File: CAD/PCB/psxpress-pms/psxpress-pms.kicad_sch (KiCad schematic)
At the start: 41 parts, among them IC1 BQ25606RGER, IC2 MAX16054AZT+T, IC3 TPS61023DRLT, IC4 TPS564255DRLR, Q1 AONR21117, SW1 SW_SPST

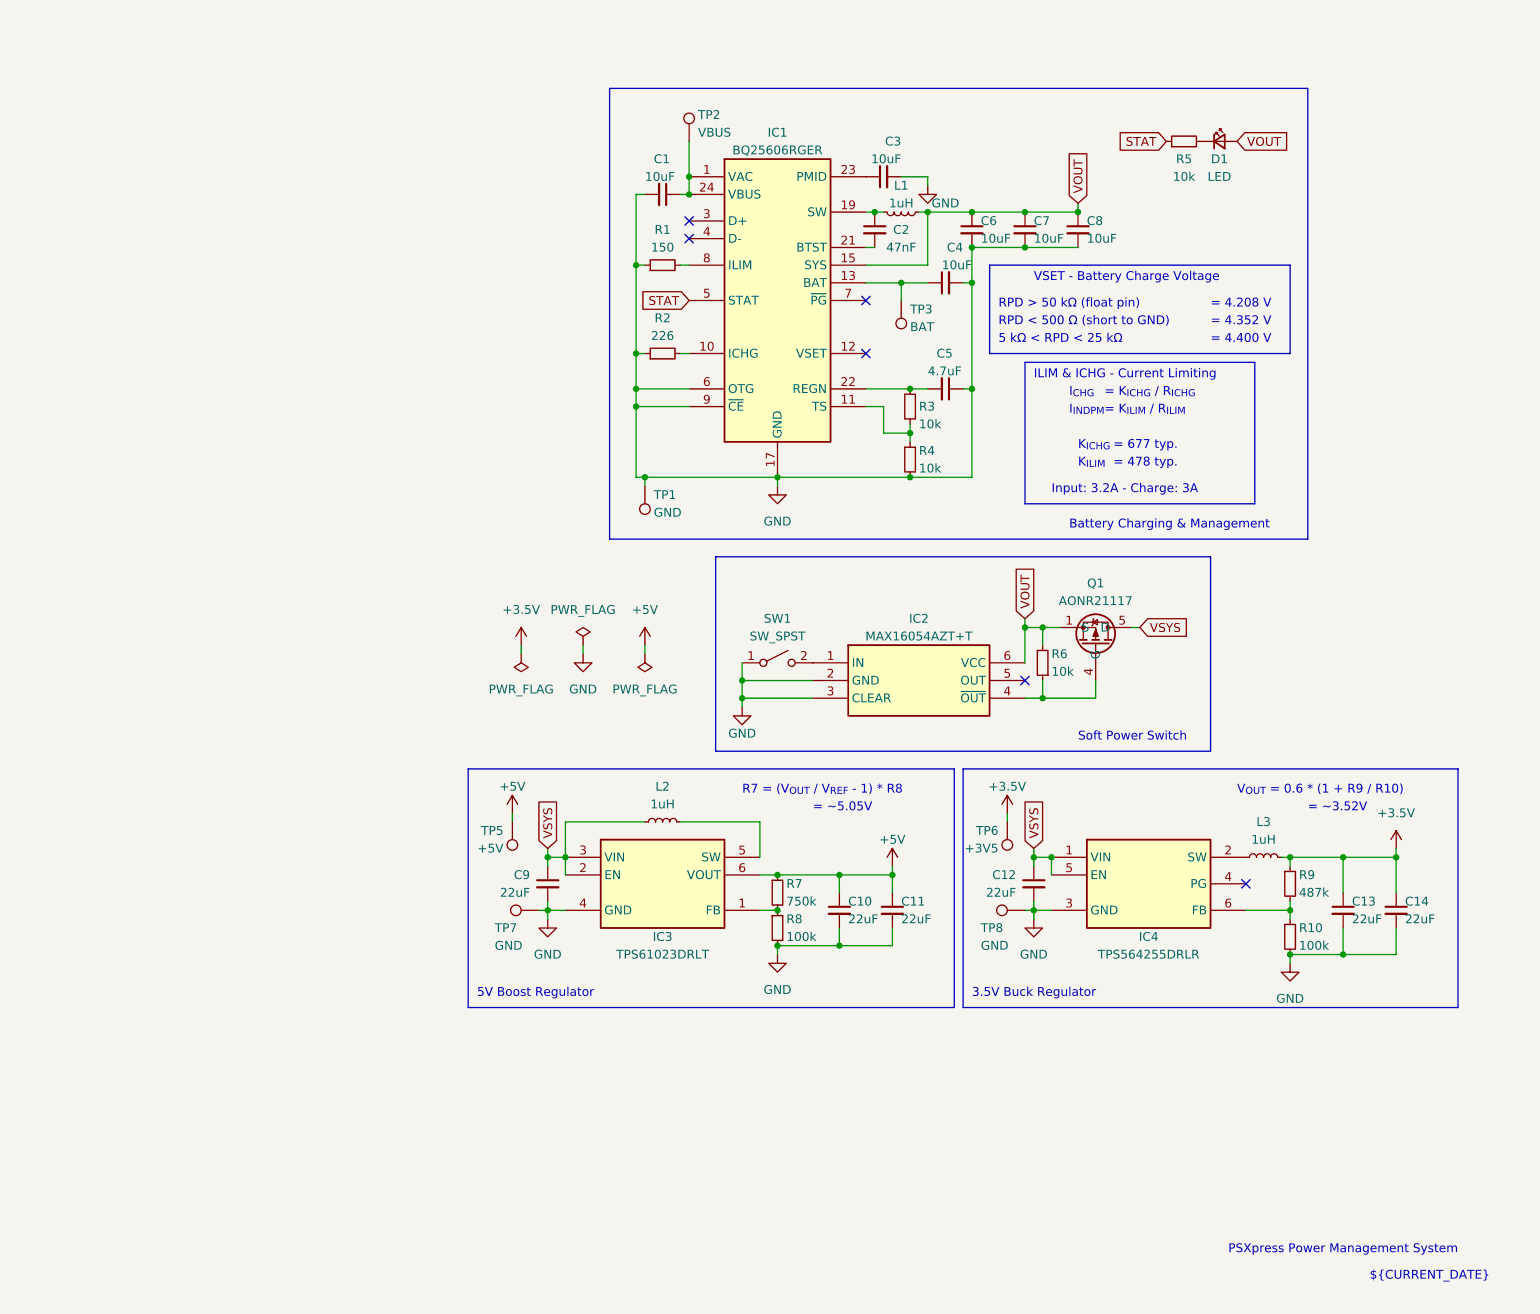
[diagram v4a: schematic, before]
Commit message: pms - switch from separate buck & boost regs to buck/boost - add todo to schematic - finish buck/boost reg schematic
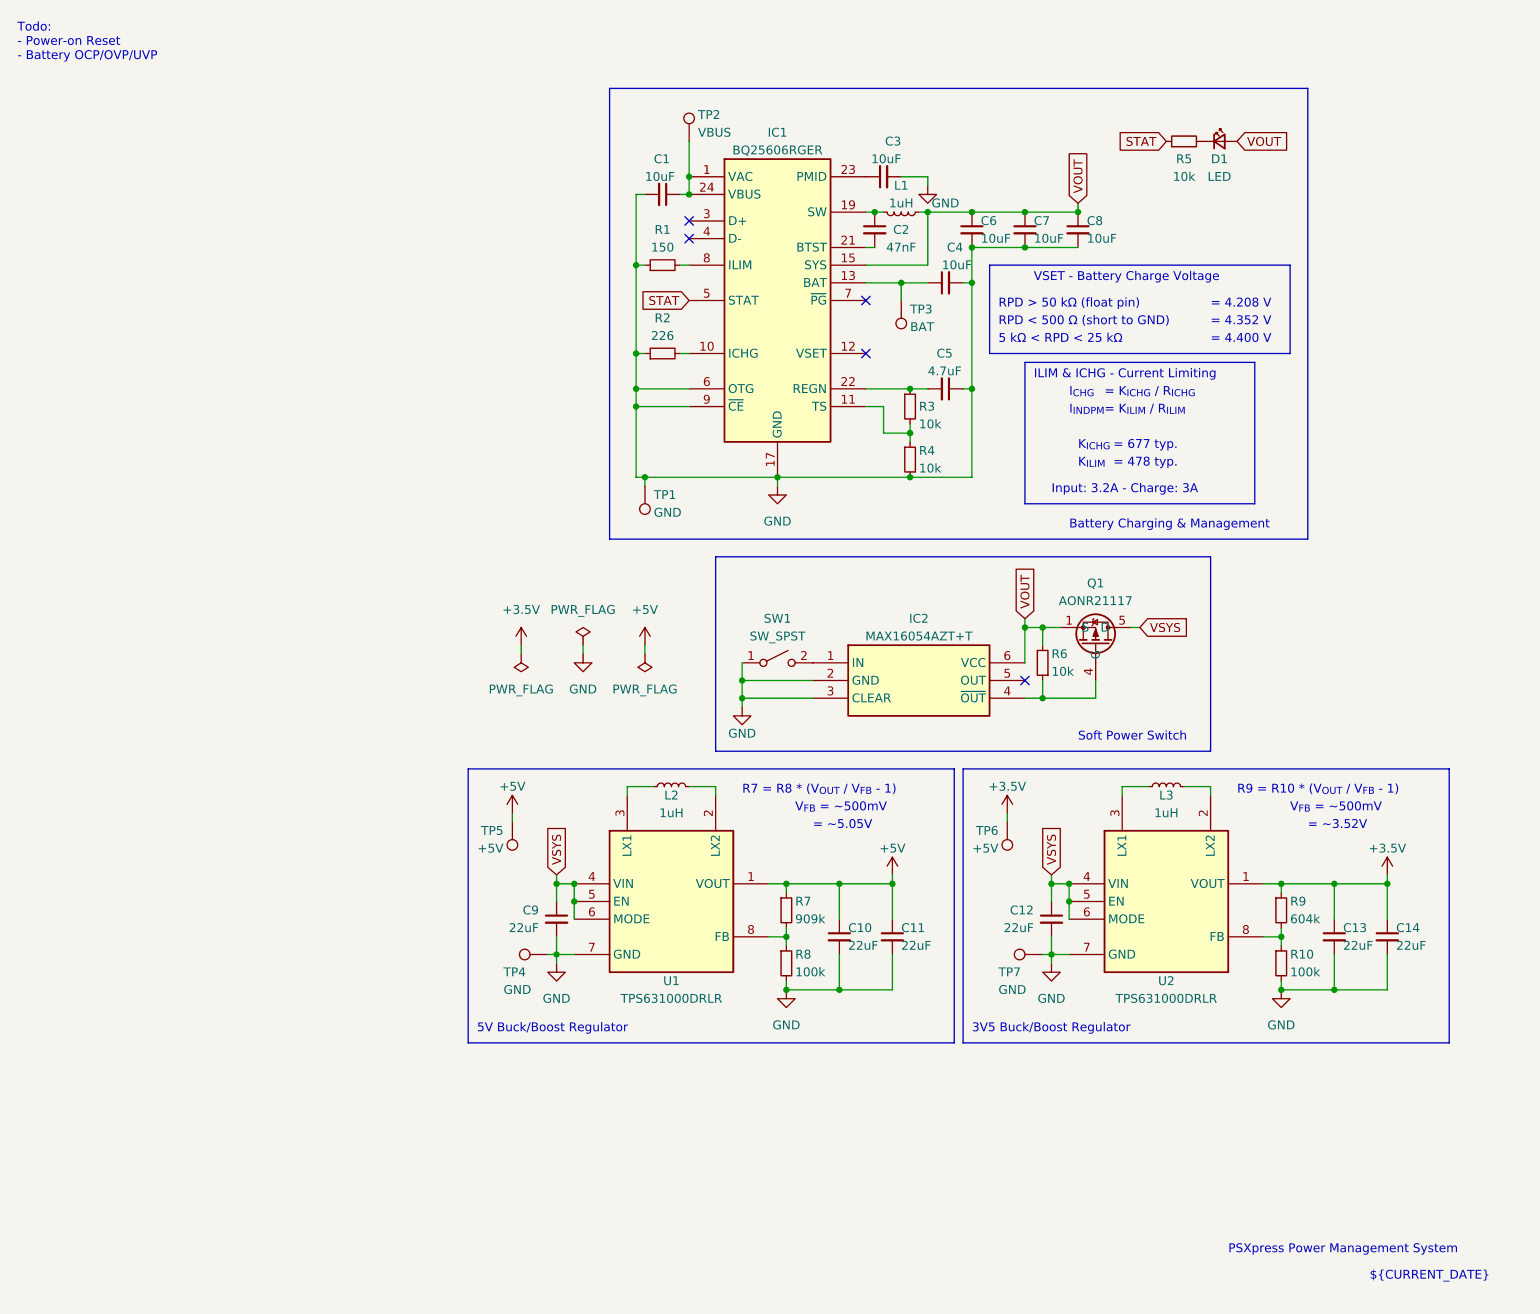
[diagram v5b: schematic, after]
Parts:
- removed IC3: TPS61023DRLT, Package_TO_SOT_SMD:SOT-666, symbol TPS61023DRLT:TPS61023DRLT
- removed IC4: TPS564255DRLR, Package_TO_SOT_SMD:SOT-666, symbol TPS564255DRLR:TPS564255DRLR
- removed TP8: GND, solderpads:hipower_2.5x1.5mm, symbol Connector:TestPoint
- added TP4: GND, solderpads:hipower_2.5x1.5mm, symbol Connector:TestPoint
- added U1, U2: TPS631000DRLR, SOTFL50P160X60-8N, symbol TPS631000DRLR:TPS631000DRLR
- R7: value 750k -> 909k
- R9: value 487k -> 604k
- TP6: value +3V5 -> +5V
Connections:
- net +3.5V: now also U2.1 (VOUT); no longer L3.2
- net +5V: now also U1.1 (VOUT)
- net GND: now also TP4.1, U1.7 (GND), U2.7 (GND)
- net VSYS: now also U1.4 (VIN), U1.5 (EN), U1.6 (MODE), U2.4 (VIN), U2.5 (EN), U2.6 (MODE); no longer L2.1
- net at R7.2, R8.1: now also U1.8 (FB)
- net at R10.1, R9.2: now also U2.8 (FB)
- net at L2.2: now also U1.2 (LX2)
- net at L3.1: now also U2.3 (LX1)
- new net: L2.1, U1.3 (LX1)
- new net: L3.2, U2.2 (LX2)
- no-connect marks 6 -> 5
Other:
- note added: "3V5 Buck/Boost Regulator"
- note added: "5V Buck/Boost Regulator"
- note added: "R7 = R8 * (V_{OUT} / V_{FB} - 1)"
- note added: "R9 = R10 * (V_{OUT} / V_{FB} - 1)"
- note added: "Todo: - Power-on Reset - Battery OCP/OVP/UVP"
- note added: "V_{FB} = ~500mV"
- note removed: "3.5V Buck Regulator"
- note removed: "5V Boost Regulator"
- note removed: "R7 = (V_{OUT} / V_{REF} - 1) * R8"
- note removed: "V_{OUT} = 0.6 * (1 + R9 / R10)"

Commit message: pms - add power-on reset circuit schematic
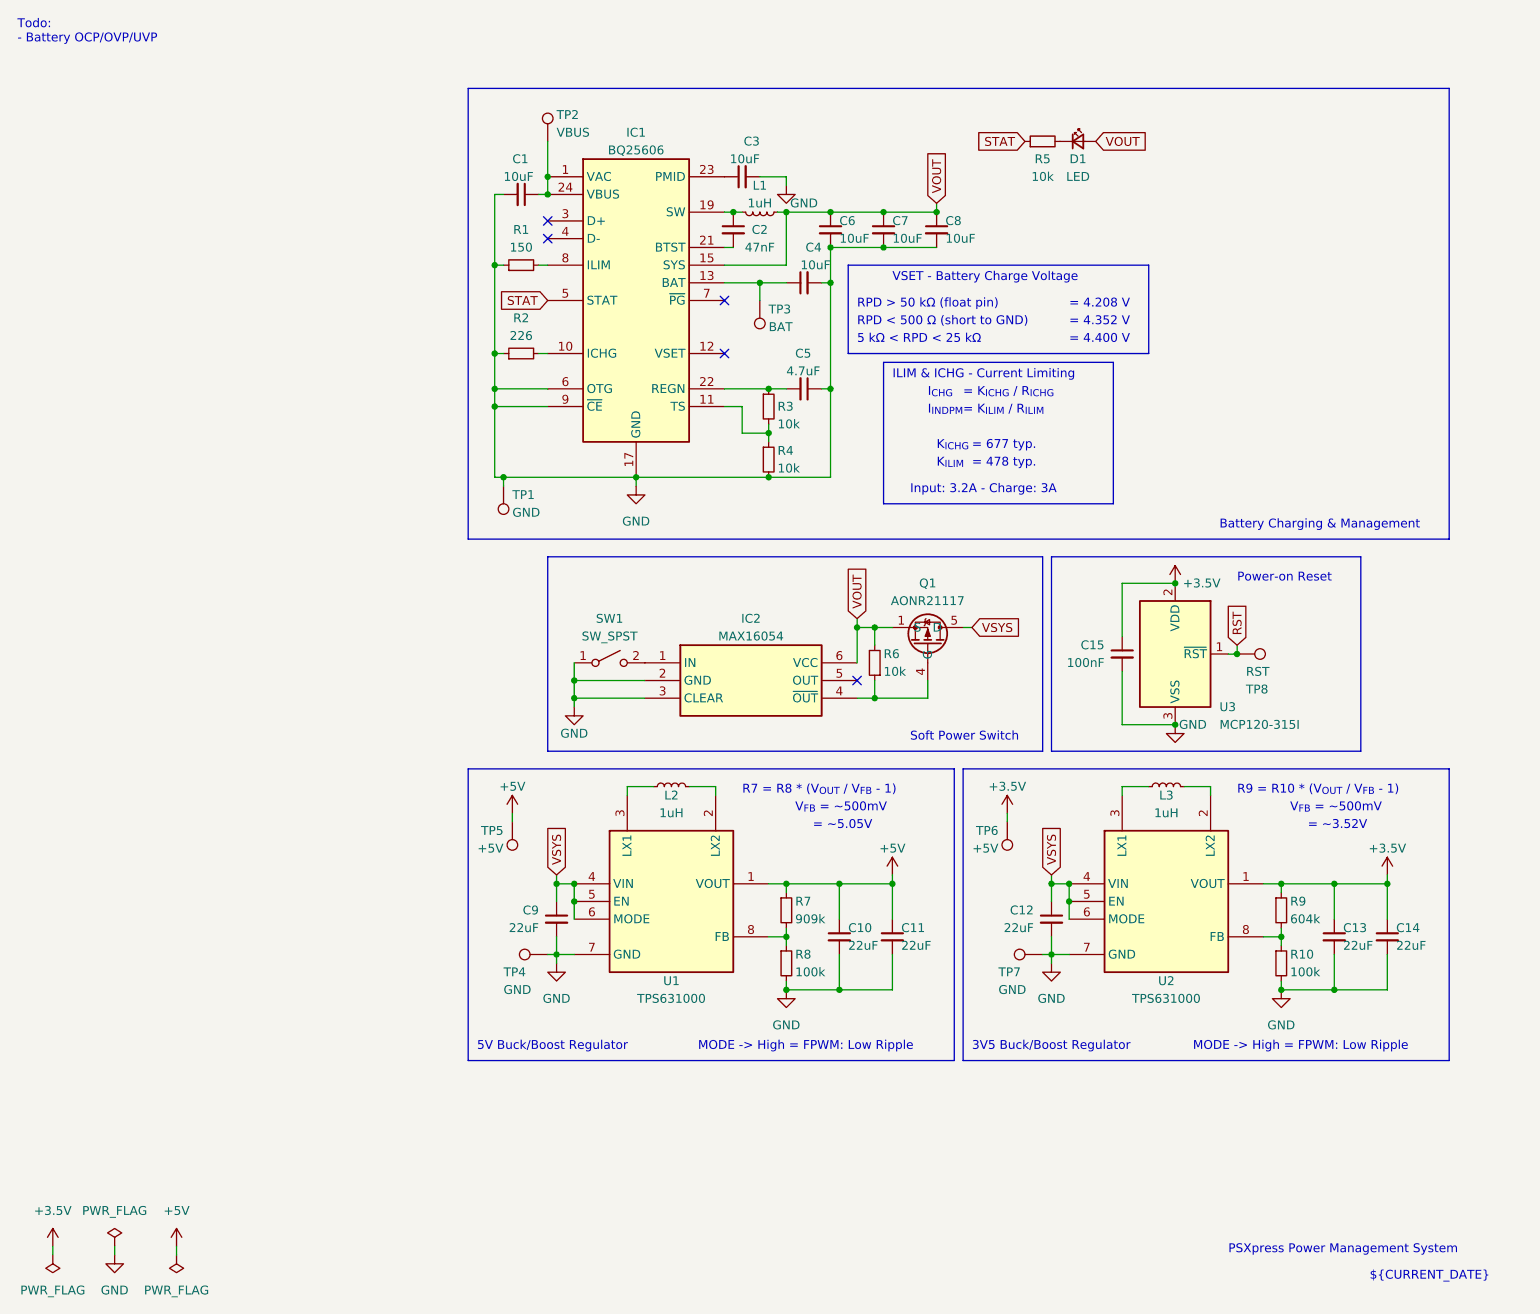
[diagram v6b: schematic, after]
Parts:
- added C15: 100nF, Capacitor_SMD:C_0805_2012Metric, symbol Device:C_Small
- added TP8: RST, solderpads:hipower_2.5x1.5mm, symbol Connector:TestPoint
- added U3: MCP120-315I, Package_TO_SOT_SMD:SOT-23, symbol Power_Supervisor:MCP120-xxxxTT
- IC1: value BQ25606RGER -> BQ25606
- IC2: value MAX16054AZT+T -> MAX16054
- U1, U2: value TPS631000DRLR -> TPS631000
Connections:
- net +3.5V: now also C15.1, U3.2 (VDD)
- net GND: now also C15.2, U3.3 (VSS)
- new net RST: TP8.1, U3.1 (~{RST})
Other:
- note added: "MODE -> High = FPWM: Low Ripple"
- note added: "Power-on Reset"
- note added: "Todo: - Battery OCP/OVP/UVP"
- note removed: "Todo: - Power-on Reset - Battery OCP/OVP/UVP"
- moved on the sheet: C1, C2, C3, C4, C5, C6, C7, C8, D1, IC1, IC2, L1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

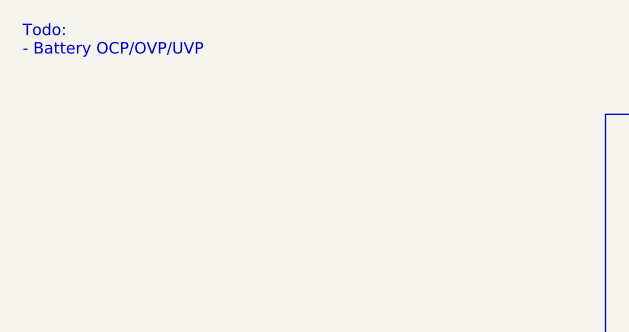
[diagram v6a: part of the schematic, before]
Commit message: pms - update schematic todo
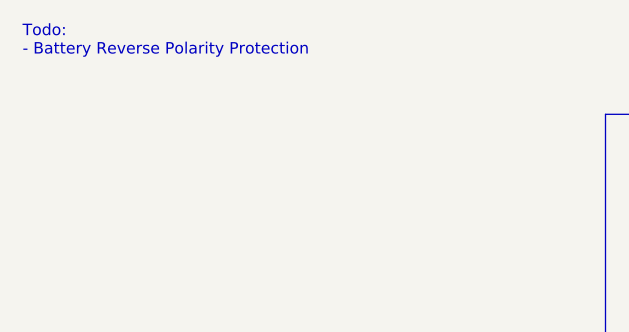
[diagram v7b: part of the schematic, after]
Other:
- note added: "Todo: - Battery Reverse Polarity Protection"
- note removed: "Todo: - Battery OCP/OVP/UVP"
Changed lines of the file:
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@@
     (effects (font (size 1.27 1.27)) (justify left bottom))
   )
-  (text "Todo: \n- Battery OCP/OVP/UVP" (at 12.7 16.51 0)
+  (text "Todo: \n- Battery Reverse Polarity Protection" (at 12.7 16.51 0)
     (effects (font (size 1.27 1.27)) (justify left bottom))
   )

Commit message: pms - finish routing new regs + POR circuit - add special thanks - awaiting cleanup
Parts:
- C15: footprint Capacitor_SMD:C_0805_2012Metric -> Capacitor_SMD:C_0603_1608Metric
- TP8: footprint solderpads:hipower_2.5x1.5mm -> solderpads:lopower_1.25mm
- U1, U2: footprint SOTFL50P160X60-8N -> Package_TO_SOT_SMD:SOT-583-8
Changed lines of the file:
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@@
       (effects (font (size 1.27 1.27)))
     )
-    (property "Footprint" "SOTFL50P160X60-8N" (at 116.84 253.67 0)
+    (property "Footprint" "Package_TO_SOT_SMD:SOT-583-8" (at 116.84 253.67 0)
       (effects (font (size 1.27 1.27)) (justify left top) hide)
     )
@@
       (effects (font (size 1.27 1.27)) (justify left))
     )
-    (property "Footprint" "solderpads:hipower_2.5x1.5mm" (at 187.96 109.22 0)
+    (property "Footprint" "solderpads:lopower_1.25mm" (at 187.96 109.22 0)
       (effects (font (size 1.27 1.27)) hide)
     )
@@
       (effects (font (size 1.27 1.27)) (justify right))
     )
-    (property "Footprint" "Capacitor_SMD:C_0805_2012Metric" (at 171.45 104.14 0)
+    (property "Footprint" "Capacitor_SMD:C_0603_1608Metric" (at 171.45 104.14 0)
       (effects (font (size 1.27 1.27)) hide)
     )
@@
       (effects (font (size 1.27 1.27)))
     )
-    (property "Footprint" "SOTFL50P160X60-8N" (at 187.96 253.67 0)
-      (effects (font (size 1.27 1.27)) (justify left top) hide)
-    )
+    (property "Footprint" "Package_TO_SOT_SMD:SOT-583-8" (at 187.96 253.67 0)
+      (effects (font (size 1.27 1.27)) (justify left top) hide)
+    )
